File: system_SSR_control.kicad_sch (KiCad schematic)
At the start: 15 parts, among them J1 171857-0003, J2 171856-0002, J3 171857-0003, Q1 2.1V, Q2 2N7000, Q3 2N7000, SW1 FSM2JSMA, SW2 FSM2JSMA

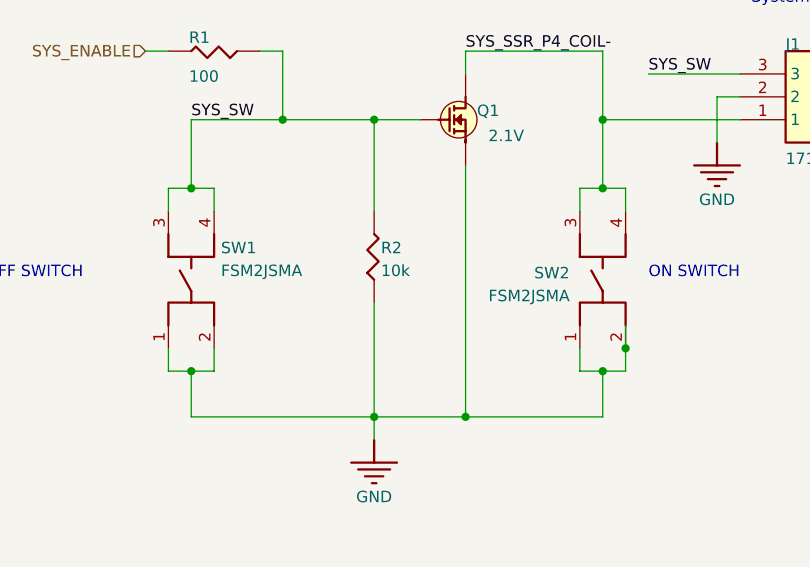
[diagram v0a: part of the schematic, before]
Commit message: Cleanup symbol field table
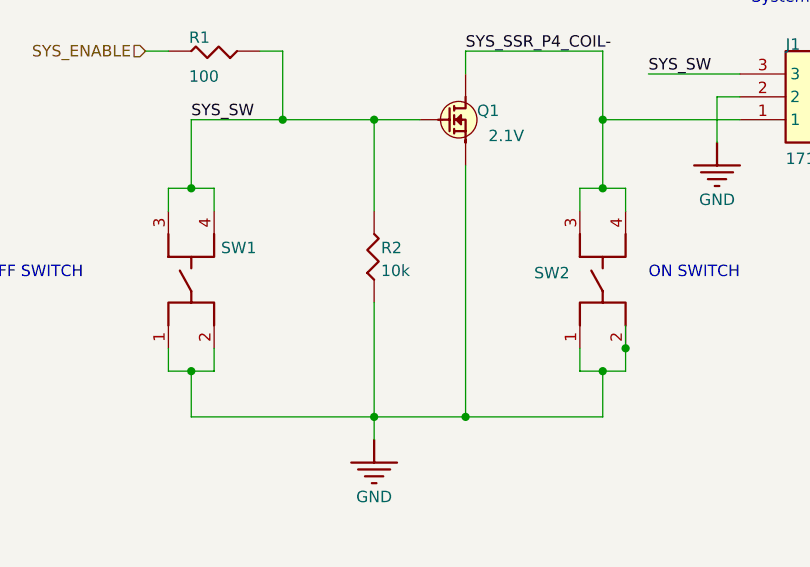
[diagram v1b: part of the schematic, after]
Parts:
- D1: ALTIUM_VALUE 1.9V -> (none); DATASHEET LINK https://www.we-online.com/katalog/datasheet/150080SS75000.p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 -> (none); MANUFACTURER Würth Elektronik -> (none); MANUFACTURER PART NUMBER 150080SS75000 -> (none); OPERATING TEMPERATURE -40°C ~ 85°C -> (none); PACKAGE / CASE 0805 (2012 Metric) -> (none); Part Number (none) -> 150080SS75000; ROHS YES -> (none)
- J1, J3: ALTIUM_VALUE 1x3 -> (none); DATASHEET LINK https://componentsearchengine.com//171857-0003.pdf -> (none); MANUFACTURER Molex -> (none); MANUFACTURER PART NUMBER 171857-0003 -> (none); MANUFACTURER_NAME Molex -> (none); MOUSER2 PART NUMBER 538-171857-0003 -> (none); MOUSER2 PRICE/STOCK https://www.mouser.com/Search/Refine.aspx?Keyword=538-17185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 -> (none); Part Number (none) -> 171857-0003
- J2: ALTIUM_VALUE 1x2 -> (none); DATASHEET LINK https://componentsearchengine.com//171856-0002.pdf -> (none); HEIGHT 8.18mm -> (none); MANUFACTURER Molex -> (none); MANUFACTURER PART NUMBER 171856-0002 -> (none); MANUFACTURER_NAME Molex -> (none); MOUSER2 PART NUMBER 538-171856-0002 -> (none); MOUSER2 PRICE/STOCK https://www.mouser.com/Search/Refine.aspx?Keyword=538-17185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 -> (none); Part Number (none) -> 171856-0002
- Q1: ALTIUM_VALUE 2.1V -> (none); DATASHEET LINK https://assets.nexperia.com/documents/data-sheet/NX7002BK.p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 -> (none); MANUFACTURER Nexperia USA Inc. -> (none); MANUFACTURER PART NUMBER NX7002BKR -> (none); OPERATING TEMPERATURE -55°C ~ 150°C -> (none); PACKAGE / CASE SOT-23-3 -> (none); Part Number (none) -> NX7002BKR; ROHS YES -> (none)
- Q2, Q3: ALTIUM_VALUE 1V -> (none); DATASHEET LINK http://www.onsemi.com/pub_link/Collateral/2N7000-D.PDF -> (none); MANUFACTURER On Semiconductor -> (none); MANUFACTURER PART NUMBER 2N7000 -> (none); OPERATING TEMPERATURE -55°C ~ 150°C -> (none); PACKAGE / CASE TO-92 -> (none); Part Number (none) -> 2N7000; ROHS YES -> (none)
- R1: ALTIUM_VALUE 100 -> (none); DATASHEET LINK https://www.yageo.com/upload/media/product/productsearch/da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 -> (none); MANUFACTURER YAGEO -> (none); MANUFACTURER PART NUMBER RC0805FR-07100RL -> (none); OPERATING TEMPERATURE -55°C ~ 155°C -> (none); PACKAGE / CASE 0805 (2012 Metric) -> (none); Part Number (none) -> RC0805FR-07100RL; ROHS YES -> (none)
- R2: ALTIUM_VALUE 10k -> (none); DATASHEET LINK https://www.yageo.com/upload/media/product/productsearch/da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 -> (none); MANUFACTURER YAGEO -> (none); MANUFACTURER PART NUMBER RC0805JR-0710KL -> (none); OPERATING TEMPERATURE -55°C ~ 155°C -> (none); PACKAGE / CASE 0805 (2012 Metric) -> (none); Part Number (none) -> RC0805JR-0710KL; ROHS YES -> (none)
- R3, R5: ALTIUM_VALUE 100k -> (none); DATASHEET LINK http://industrial.panasonic.com/www-cgi/jvcr13pz.cgi?E+PZ+3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 -> (none); MANUFACTURER Panasonic Electronic Components -> (none); MANUFACTURER PART NUMBER ERJ-6ENF1003V -> (none); OPERATING TEMPERATURE -55°C ~ 155°C -> (none); PACKAGE / CASE 0805 (2012 Metric) -> (none); Part Number (none) -> ERJ-6ENF1003V; ROHS YES -> (none)
- R4: ALTIUM_VALUE 140 -> (none); DATASHEET LINK https://www.yageo.com/upload/media/product/productsearch/da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 -> (none); MANUFACTURER YAGEO -> (none); MANUFACTURER PART NUMBER RC0805FR-07140RL -> (none); OPERATING TEMPERATURE -55°C ~ 155°C -> (none); PACKAGE / CASE 0805 (2012 Metric) -> (none); Part Number (none) -> RC0805FR-07140RL; ROHS YES -> (none)
- R6: @ QTY 1500 -> (none); ALTIUM_VALUE 100k -> (none); COMPOSITION Thick Film -> (none); DATASHEETS http://industrial.panasonic.com/www-cgi/jvcr13pz.cgi?E+PZ+3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 -> (none); DIGI-KEY PART NUMBER P100KCCT-ND -> (none); FACTORY STOCK 0 -> (none); FAILURE RATE - -> (none); FEATURES Automotive AEC-Q200 -> (none); HEIGHT - SEATED (MAX) 0.028" (0.70mm) -> (none); IMAGE //media.digikey.com/Renders/Panasonic%20Renders/ERJ-0805%20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 -> (none); MANUFACTURER Panasonic Electronic Components -> (none); MANUFACTURER PART NUMBER ERJ-6ENF1003V -> (none); MINIMUM QUANTITY 1 -> (none); NUMBER OF TERMINATIONS 2 -> (none); OPERATING TEMPERATURE -55°C ~ 155°C -> (none); PACKAGE / CASE 0805 (2012 Metric) -> (none); PACKAGING Cut Tape (CT) -> (none); PART NUMBER ERJ-6ENF1003V -> (none); PART STATUS Active -> (none); POWER (WATTS) 0.125W, 1/8W -> (none); Part Number (none) -> ERJ-6ENF1003V; QUANTITY AVAILABLE 760677 -> (none); SERIES ERJ -> (none); SIZE / DIMENSION 0.079" L x 0.049" W (2.00mm x 1.25mm) -> (none); SUPPLIER DEVICE PACKAGE 0805 -> (none); TEMPERATURE COEFFICIENT ±100ppm/°C -> (none); TOLERANCE ±1% -> (none); UNIT PRICE (USD) 0.00729 -> (none)
- SW1, SW2: ALTIUM_VALUE 24V -> (none); DATASHEET LINK https://www.te.com/commerce/DocumentDelivery/DDEController?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 -> (none); MANUFACTURER TE Connectivity -> (none); MANUFACTURER PART NUMBER FSM2JSMA -> (none); OPERATING TEMPERATURE -35°C ~ 85°C -> (none); PACKAGE / CASE Non-standard -> (none); Part Number (none) -> FSM2JSMA; ROHS YES -> (none)

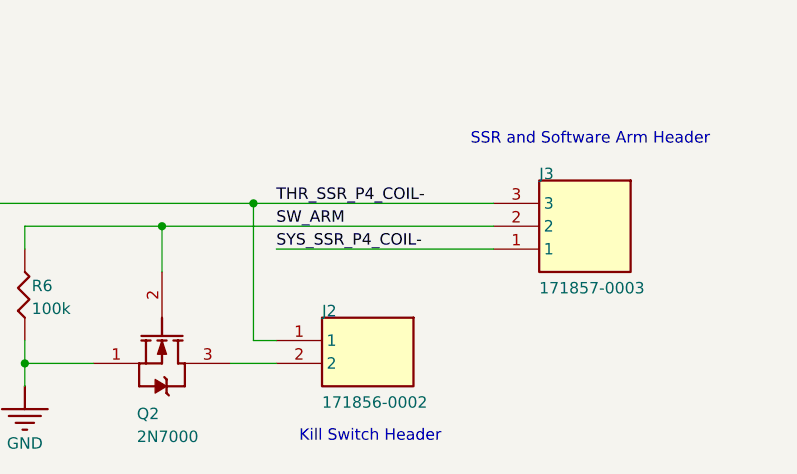
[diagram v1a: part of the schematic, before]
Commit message: Input and Output Header Updates to MEB
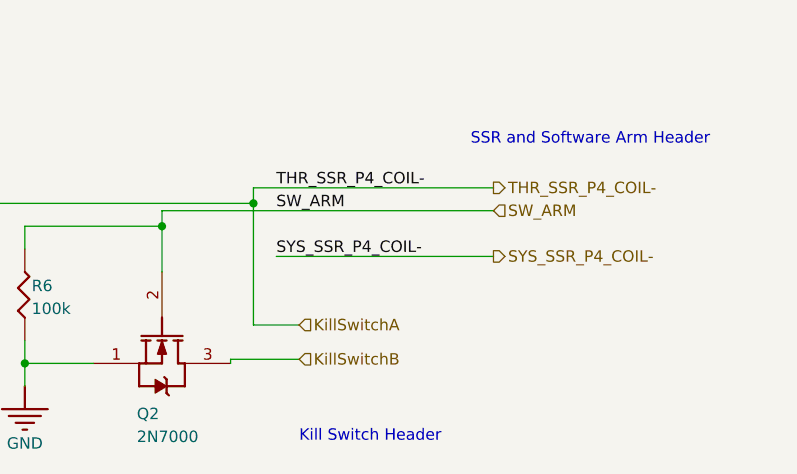
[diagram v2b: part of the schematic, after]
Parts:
- removed J2: 171856-0002, AltiumImport:SHDR2W99P0X254_1X2_493X635X818P, symbol MEB-altium-import:system_SSR_control_0_171856-0002
- removed J3: 171857-0003, AltiumImport:171857-0003, symbol MEB-altium-import:system_SSR_control_0_171857-0003
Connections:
- net KillSwitchB: now reaches Q2.3 (D)
- net THR_SSR_P4_COIL- renamed KillSwitchA
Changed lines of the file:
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@@
   (junction (at 165.1 83.0072) (diameter 0) (color 0 0 0 0)
   )
-  (wire (pts (xy 198.12 169.3672) (xy 195.58 169.3672))
+  (wire (pts (xy 200.66 167.64) (xy 195.58 167.64))
     (stroke (width 0.254) (type default))
   )
@@
     (stroke (width 0.254) (type default))
   )
-  (wire (pts (xy 198.12 171.9072) (xy 193.04 171.9072))
+  (wire (pts (xy 193.04 171.45) (xy 200.66 171.45))
     (stroke (width 0.254) (type default))
   )
@@
     (stroke (width 0.254) (type default))
   )
-  (wire (pts (xy 222.25 159.2072) (xy 198.12 159.2072))
+  (wire (pts (xy 222.25 160.02) (xy 198.12 160.02))
     (stroke (width 0.254) (type default))
   )
@@
     (stroke (width 0.254) (type default))
   )
-  (wire (pts (xy 185.42 156.6672) (xy 222.25 156.6672))
+  (wire (pts (xy 185.42 154.94) (xy 222.25 154.94))
     (stroke (width 0.254) (type default))
   )
@@
     (stroke (width 0.254) (type default))
   )
-  (wire (pts (xy 195.58 169.3672) (xy 195.58 154.1272))
+  (wire (pts (xy 195.58 167.64) (xy 195.58 154.1272))
     (stroke (width 0.254) (type default))
   )
@@
     (stroke (width 0.254) (type default))
   )
+  (wire (pts (xy 193.04 171.45) (xy 193.04 171.9072))
+    (stroke (width 0.254) (type default))
+  )
   (wire (pts (xy 165.1 83.0072) (xy 165.1 75.3872))
     (stroke (width 0.254) (type default))
@@
     (stroke (width 0.254) (type default))
   )
+  (wire (pts (xy 185.42 154.94) (xy 185.42 156.6672))
+    (stroke (width 0.254) (type default))
+  )
   (wire (pts (xy 144.78 83.0072) (xy 139.7 83.0072))
     (stroke (width 0.254) (type default))
@@
     (stroke (width 0.254) (type default))
   )
-  (wire (pts (xy 195.58 154.1272) (xy 222.25 154.1272))
+  (wire (pts (xy 195.58 152.4) (xy 222.25 152.4))
     (stroke (width 0.254) (type default))
   )
@@
   )
   (wire (pts (xy 121.92 110.9472) (xy 121.92 108.4072))
+    (stroke (width 0.254) (type default))
+  )
+  (wire (pts (xy 195.58 152.4) (xy 195.58 154.1272))
     (stroke (width 0.254) (type default))
   )
@@
     (effects (font (size 1.27 1.27)) (justify left bottom))
   )
-  (label "THR_SSR_P4_COIL-" (at 198.12 154.1272 0) (fields_autoplaced)
-    (effects (font (size 1.27 1.27)) (justify left bottom))
-  )
-  (label "SYS_SSR_P4_COIL-" (at 198.12 159.2072 0) (fields_autoplaced)
-    (effects (font (size 1.27 1.27)) (justify left bottom))
-  )
-  (label "SW_ARM" (at 198.12 156.6672 0) (fields_autoplaced)
+  (label "THR_SSR_P4_COIL-" (at 198.12 152.4 0) (fields_autoplaced)
+    (effects (font (size 1.27 1.27)) (justify left bottom))
+  )
+  (label "SYS_SSR_P4_COIL-" (at 198.12 160.02 0) (fields_autoplaced)
+    (effects (font (size 1.27 1.27)) (justify left bottom))
+  )
+  (label "SW_ARM" (at 198.12 154.94 0) (fields_autoplaced)
     (effects (font (size 1.27 1.27)) (justify left bottom))
   )
   (label "SYS_SW" (at 170.18 77.9272 0) (fields_autoplaced)
     (effects (font (size 1.27 1.27)) (justify left bottom))
+  )
+  (hierarchical_label "KillSwitchA" (shape input) (at 200.66 167.64 0) (fields_autoplaced)
+    (effects (font (size 1.27 1.27)) (justify left))
+  )
+  (hierarchical_label "SYS_SSR_P4_COIL-" (shape output) (at 222.25 160.02 0) (fields_autoplaced)
+    (effects (font (size 1.27 1.27)) (justify left))
   )
   (hierarchical_label "THR_KILLED" (shape output) (at 86.36 161.7472 180) (fields_autoplaced)
     (effects (font (size 1.27 1.27)) (justify right))
   )
+  (hierarchical_label "KillSwitchB" (shape input) (at 200.66 171.45 0) (fields_autoplaced)
+    (effects (font (size 1.27 1.27)) (justify left))
+  )
+  (hierarchical_label "THR_SSR_P4_COIL-" (shape output) (at 222.25 152.4 0) (fields_autoplaced)
+    (effects (font (size 1.27 1.27)) (justify left))
+  )
   (hierarchical_label "SYS_ENABLE" (shape input) (at 114.3 75.3872 180) (fields_autoplaced)
     (effects (font (size 1.27 1.27)) (justify right))
+  )
+  (hierarchical_label "SW_ARM" (shape input) (at 222.25 154.94 0) (fields_autoplaced)
+    (effects (font (size 1.27 1.27)) (justify left))
   )
   (symbol (lib_id "MEB-altium-import:GND") (at 170.18 174.4472 0) (unit 1)
@@
         )
       )
-    )
-  )
-  (symbol (lib_id "MEB-altium-import:system_SSR_control_0_171856-0002") (at 198.12 169.3672 0) (unit 1)
-    (in_bom yes) (on_board yes) (dnp no)
-    (property "Reference" "J2" (at 203.2 166.8272 0)
-      (effects (font (size 1.27 1.27)) (justify left bottom))
-    )
-    (property "Value" "171856-0002" (at 203.2 176.9872 0)
-      (effects (font (size 1.27 1.27)) (justify left bottom))
-    )
-    (property "Footprint" "AltiumImport:SHDR2W99P0X254_1X2_493X635X818P" (at 198.12 169.3672 0)
-      (effects (font (size 1.27 1.27)) hide)
-    )
-    (property "Datasheet" "" (at 198.12 169.3672 0)
-      (effects (font (size 1.27 1.27)) hide)
-    )
-    (property "Part Number" "171856-0002" (at 198.12 169.3672 0)
-      (effects (font (size 1.27 1.27)) hide)
-    )
-    (pin "1")
-    (pin "2")
-    (instances
-      (project "MEB"
-        (path "/228e4997-23c1-4c21-939b-583cad26a5e3/d2748488-1aa2-4890-bfa9-60c09f864312"
-          (reference "J2") (unit 1)
-        )
-      )
-    )
-  )
-  (symbol (lib_id "MEB-altium-import:system_SSR_control_0_171857-0003") (at 222.25 154.1272 0) (unit 1)
-    (in_bom yes) (on_board yes) (dnp no)
-    (property "Reference" "J3" (at 227.33 151.5872 0)
-      (effects (font (size 1.27 1.27)) (justify left bottom))
-    )
-    (property "Value" "171857-0003" (at 227.33 164.2872 0)
-      (effects (font (size 1.27 1.27)) (justify left bottom))
-    )
-    (property "Footprint" "AltiumImport:171857-0003" (at 222.25 154.1272 0)
-      (effects (font (size 1.27 1.27)) hide)
-    )
-    (property "Datasheet" "" (at 222.25 154.1272 0)
-      (effects (font (size 1.27 1.27)) hide)
-    )
-    (property "Part Number" "171857-0003" (at 222.25 154.1272 0)
-      (effects (font (size 1.27 1.27)) hide)
-    )
-    (pin "1")
-    (pin "2")
-    (pin "3")
-    (instances
-      (project "MEB"
-        (path "/228e4997-23c1-4c21-939b-583cad26a5e3/d2748488-1aa2-4890-bfa9-60c09f864312"
-          (reference "J3") (unit 1)
-        )
-      )
